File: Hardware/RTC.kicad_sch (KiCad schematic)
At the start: 15 parts, among them IC1 RTC_DS3231M, U7 PCF8563TS, Y1 32.768kHz

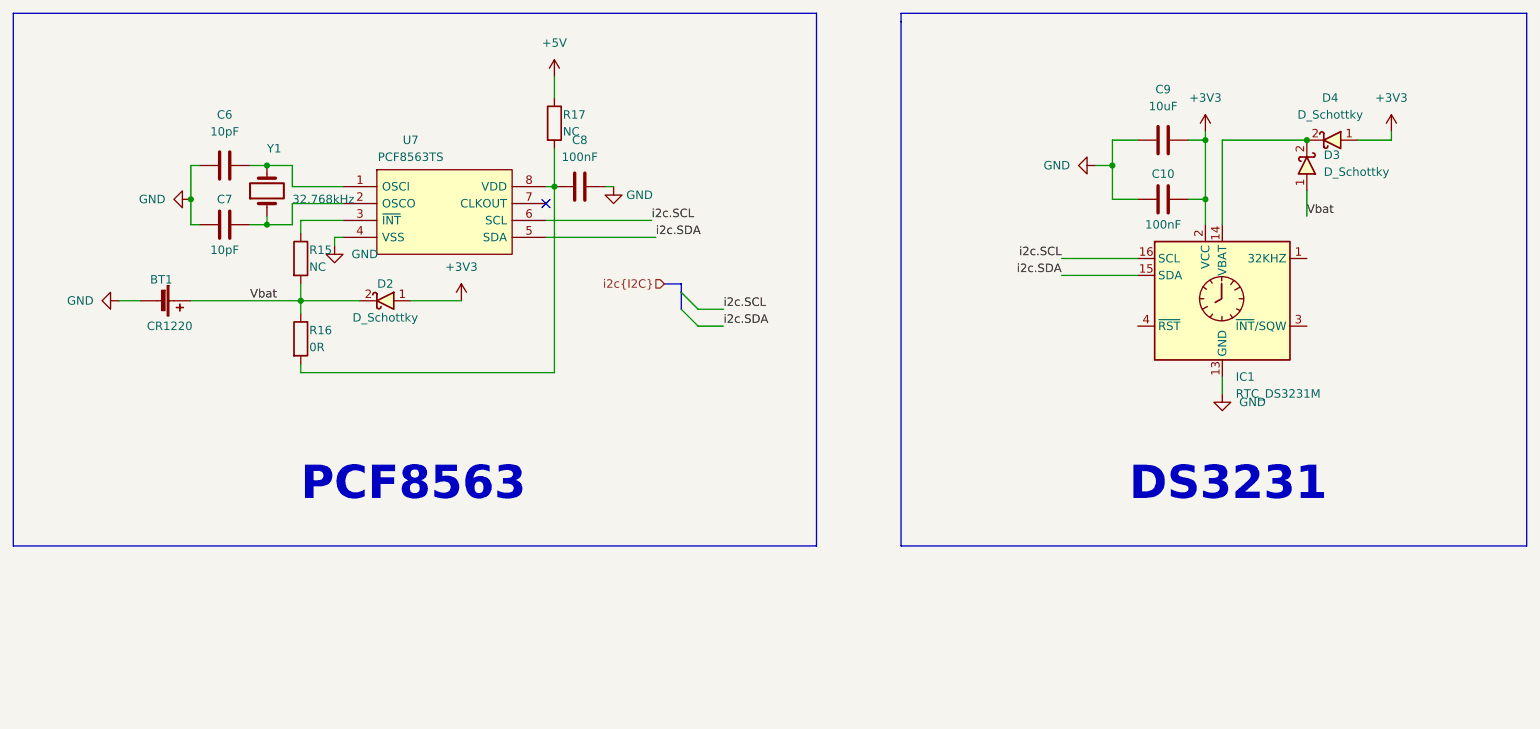
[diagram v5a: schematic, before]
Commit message: fix MCP41010, fix symbol output header
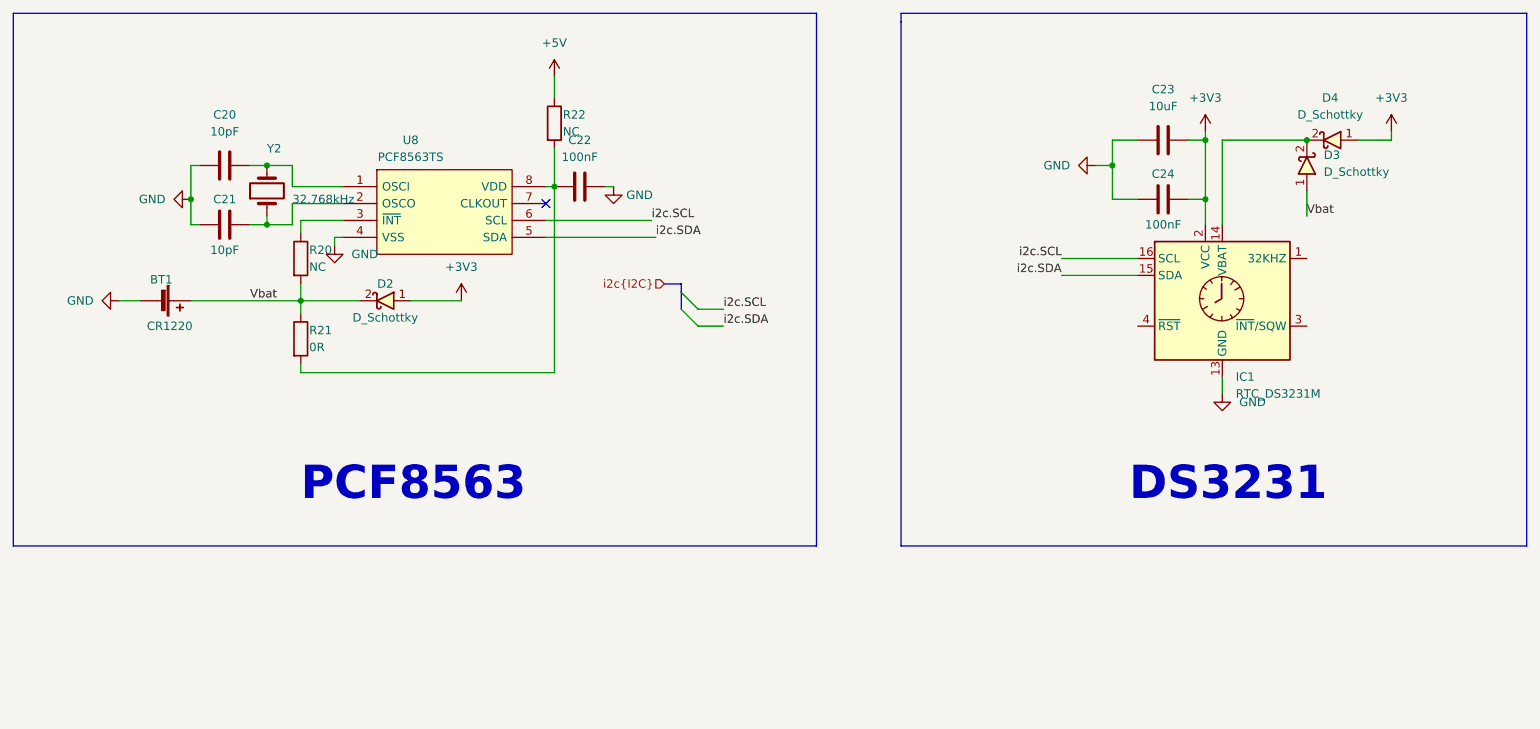
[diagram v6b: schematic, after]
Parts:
- D2, D3, D4: footprint (none) -> IVS_FOOTPRINTS:D_SMA
- renumbered C6 to C20, C7 to C21, C8 to C22, C9 to C23, C10 to C24, R15 to R20, R16 to R21, R17 to R22, U7 to U8, Y1 to Y2
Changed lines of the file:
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@@
     (property "Reference" "D4" (id 0) (at 234.6494 36.83 0))
     (property "Value" "D_Schottky" (id 1) (at 234.6494 39.37 0))
-    (property "Footprint" "" (id 2) (at 233.68 43.18 0)
+    (property "Footprint" "IVS_FOOTPRINTS:D_SMA" (id 2) (at 233.68 43.18 0)
       (effects (font (size 1.27 1.27)) hide)
     )
@@
       (effects (font (size 1.27 1.27)) (justify left))
     )
-    (property "Footprint" "" (id 2) (at 231.14 45.72 0)
+    (property "Footprint" "IVS_FOOTPRINTS:D_SMA" (id 2) (at 231.14 45.72 0)
       (effects (font (size 1.27 1.27)) hide)
     )
@@
   (symbol (lib_id "Device:Crystal") (at 74.93 50.8 90) (unit 1)
     (in_bom yes) (on_board yes)
-    (property "Reference" "Y1" (id 0) (at 74.93 44.45 90)
+    (property "Reference" "Y2" (id 0) (at 74.93 44.45 90)
       (effects (font (size 1.27 1.27)) (justify right))
     )
@@
   (symbol (lib_id "power:GND") (at 85.09 59.055 0) (unit 1)
     (in_bom yes) (on_board yes) (fields_autoplaced)
-    (property "Reference" "#PWR0144" (id 0) (at 85.09 65.405 0)
+    (property "Reference" "#PWR050" (id 0) (at 85.09 65.405 0)
       (effects (font (size 1.27 1.27)) hide)
     )
@@
   (symbol (lib_id "Device:C") (at 209.55 52.07 90) (unit 1)
     (in_bom yes) (on_board yes)
-    (property "Reference" "C10" (id 0) (at 209.55 48.26 90))
+    (property "Reference" "C24" (id 0) (at 209.55 48.26 90))
     (property "Value" "100nF" (id 1) (at 209.55 55.88 90))
     (property "Footprint" "IVS_FOOTPRINTS:C0603" (id 2) (at 213.36 51.1048 0)
@@
   (symbol (lib_id "Device:C") (at 68.58 55.88 90) (unit 1)
     (in_bom yes) (on_board yes)
-    (property "Reference" "C7" (id 0) (at 68.58 52.07 90))
+    (property "Reference" "C21" (id 0) (at 68.58 52.07 90))
     (property "Value" "10pF" (id 1) (at 68.58 59.69 90))
     (property "Footprint" "IVS_FOOTPRINTS:C0603" (id 2) (at 72.39 54.9148 0)
@@
   (symbol (lib_id "power:GND") (at 63.5 52.07 270) (unit 1)
     (in_bom yes) (on_board yes) (fields_autoplaced)
-    (property "Reference" "#PWR0143" (id 0) (at 57.15 52.07 0)
+    (property "Reference" "#PWR049" (id 0) (at 57.15 52.07 0)
       (effects (font (size 1.27 1.27)) hide)
     )
@@
   (symbol (lib_id "Device:R") (at 118.11 40.64 0) (unit 1)
     (in_bom yes) (on_board yes)
-    (property "Reference" "R17" (id 0) (at 119.38 39.37 0)
+    (property "Reference" "R22" (id 0) (at 119.38 39.37 0)
       (effects (font (size 1.27 1.27)) (justify left))
     )
@@
   (symbol (lib_id "Device:C") (at 121.92 50.165 90) (unit 1)
     (in_bom yes) (on_board yes) (fields_autoplaced)
-    (property "Reference" "C8" (id 0) (at 121.92 43.18 90))
+    (property "Reference" "C22" (id 0) (at 121.92 43.18 90))
     (property "Value" "100nF" (id 1) (at 121.92 45.72 90))
     (property "Footprint" "IVS_FOOTPRINTS:C0603" (id 2) (at 125.73 49.1998 0)
@@
     (property "Reference" "D2" (id 0) (at 92.71 64.77 0))
     (property "Value" "D_Schottky" (id 1) (at 92.71 69.85 0))
-    (property "Footprint" "" (id 2) (at 91.44 67.31 0)
+    (property "Footprint" "IVS_FOOTPRINTS:D_SMA" (id 2) (at 91.44 67.31 0)
       (effects (font (size 1.27 1.27)) hide)
     )
@@
   (symbol (lib_id "power:+5V") (at 118.11 33.655 0) (unit 1)
     (in_bom yes) (on_board yes) (fields_autoplaced)
-    (property "Reference" "#PWR0147" (id 0) (at 118.11 37.465 0)
+    (property "Reference" "#PWR052" (id 0) (at 118.11 37.465 0)
       (effects (font (size 1.27 1.27)) hide)
     )
@@
   (symbol (lib_id "project:PCF8563TS") (at 101.6 53.975 0) (unit 1)
     (in_bom yes) (on_board yes)
-    (property "Reference" "U7" (id 0) (at 96.52 43.18 0))
+    (property "Reference" "U8" (id 0) (at 96.52 43.18 0))
     (property "Value" "PCF8563TS" (id 1) (at 91.44 79.375 0)
       (effects (font (size 1.27 1.27)) (justify left) hide)
@@
   (symbol (lib_id "power:+3V3") (at 215.9 41.91 0) (unit 1)
     (in_bom yes) (on_board yes) (fields_autoplaced)
-    (property "Reference" "#PWR0130" (id 0) (at 215.9 45.72 0)
+    (property "Reference" "#PWR055" (id 0) (at 215.9 45.72 0)
       (effects (font (size 1.27 1.27)) hide)
     )
@@
   (symbol (lib_id "Device:C") (at 209.55 43.18 90) (unit 1)
     (in_bom yes) (on_board yes) (fields_autoplaced)
-    (property "Reference" "C9" (id 0) (at 209.55 35.56 90))
+    (property "Reference" "C23" (id 0) (at 209.55 35.56 90))
     (property "Value" "10uF" (id 1) (at 209.55 38.1 90))
     (property "Footprint" "IVS_FOOTPRINTS:C0603" (id 2) (at 213.36 42.2148 0)
@@
   (symbol (lib_id "power:GND") (at 127 50.165 0) (unit 1)
     (in_bom yes) (on_board yes) (fields_autoplaced)
-    (property "Reference" "#PWR0148" (id 0) (at 127 56.515 0)
+    (property "Reference" "#PWR053" (id 0) (at 127 56.515 0)
       (effects (font (size 1.27 1.27)) hide)
     )
@@
   (symbol (lib_id "power:+3V3") (at 243.84 41.91 0) (unit 1)
     (in_bom yes) (on_board yes) (fields_autoplaced)
-    (property "Reference" "#PWR0133" (id 0) (at 243.84 45.72 0)
+    (property "Reference" "#PWR057" (id 0) (at 243.84 45.72 0)
       (effects (font (size 1.27 1.27)) hide)
     )
@@
   (symbol (lib_id "power:GND") (at 199.39 46.99 270) (unit 1)
     (in_bom yes) (on_board yes) (fields_autoplaced)
-    (property "Reference" "#PWR0132" (id 0) (at 193.04 46.99 0)
+    (property "Reference" "#PWR054" (id 0) (at 193.04 46.99 0)
       (effects (font (size 1.27 1.27)) hide)
     )
@@
   (symbol (lib_id "power:+3V3") (at 104.14 67.31 0) (unit 1)
     (in_bom yes) (on_board yes) (fields_autoplaced)
-    (property "Reference" "#PWR0146" (id 0) (at 104.14 71.12 0)
+    (property "Reference" "#PWR051" (id 0) (at 104.14 71.12 0)
       (effects (font (size 1.27 1.27)) hide)
     )
@@
   (symbol (lib_id "Device:R") (at 80.01 60.96 0) (unit 1)
     (in_bom yes) (on_board yes)
-    (property "Reference" "R15" (id 0) (at 81.28 59.69 0)
+    (property "Reference" "R20" (id 0) (at 81.28 59.69 0)
       (effects (font (size 1.27 1.27)) (justify left))
     )
@@
   (symbol (lib_id "power:GND") (at 218.44 81.28 0) (unit 1)
     (in_bom yes) (on_board yes) (fields_autoplaced)
-    (property "Reference" "#PWR0138" (id 0) (at 218.44 87.63 0)
+    (property "Reference" "#PWR056" (id 0) (at 218.44 87.63 0)
       (effects (font (size 1.27 1.27)) hide)
     )
@@
   (symbol (lib_id "Device:C") (at 68.58 46.99 90) (unit 1)
     (in_bom yes) (on_board yes) (fields_autoplaced)
-    (property "Reference" "C6" (id 0) (at 68.58 39.37 90))
+    (property "Reference" "C20" (id 0) (at 68.58 39.37 90))
     (property "Value" "10pF" (id 1) (at 68.58 41.91 90))
     (property "Footprint" "IVS_FOOTPRINTS:C0603" (id 2) (at 72.39 46.0248 0)
@@
   (symbol (lib_id "Device:R") (at 80.01 73.025 0) (unit 1)
     (in_bom yes) (on_board yes)
-    (property "Reference" "R16" (id 0) (at 81.28 71.755 0)
+    (property "Reference" "R21" (id 0) (at 81.28 71.755 0)
       (effects (font (size 1.27 1.27)) (justify left))
     )
@@
   (symbol (lib_id "power:GND") (at 52.705 67.31 270) (unit 1)
     (in_bom yes) (on_board yes) (fields_autoplaced)
-    (property "Reference" "#PWR0139" (id 0) (at 46.355 67.31 0)
-      (effects (font (size 1.27 1.27)) hide)
-    )
+    (property "Reference" "#PWR048" (id 0) (at 46.355 67.31 0)
+      (effects (font (size 1.27 1.27)) hide)
+    )

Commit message: add footprint
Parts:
- Y2: footprint (none) -> Crystal:Crystal_SMD_SeikoEpson_MC306-4Pin_8.0x3.2mm
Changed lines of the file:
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@@
       (effects (font (size 1.27 1.27)) (justify right))
     )
-    (property "Footprint" "" (id 2) (at 74.93 50.8 0)
+    (property "Footprint" "Crystal:Crystal_SMD_SeikoEpson_MC306-4Pin_8.0x3.2mm" (id 2) (at 74.93 50.8 0)
       (effects (font (size 1.27 1.27)) hide)
     )
